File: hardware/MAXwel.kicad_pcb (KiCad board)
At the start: 2 copper layers, 85.9 x 94.6 mm, 155 parts, among them J1 Conn_02x05_Odd_Even, J2 Conn_02x12_Counter_Clockwise, J3 Barrel_Jack_Switch_Pin3Ring, SW1 SW_Push_Dual, SW10 SW_Wuerth_450301014042, SW11 SW_Wuerth_450301014042, SW12 SW_Wuerth_450301014042, SW13 SW_Wuerth_450301014042, SW2 SW_Push_Dual, SW3 SW_Push_Dual, SW4 SW_Push_Dual, SW5 SW_Wuerth_450301014042, SW6 SW_Wuerth_450301014042, SW7 SW_Wuerth_450301014042, SW8 SW_Wuerth_450301014042, SW9 SW_Push_DPDT, U1 D168K, U2 D168K, U3 D168K, U4 D168K, U5 EPM240T100, U6 AMS1117-3.3, X1 50.000, X2 14.756

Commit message: fill README with content + Rename project
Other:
- board text added: "MAXwel FPGA Board Michael Hohenstein"
- board text removed: "MAXwell FPGA Board Michael Hohenstein"

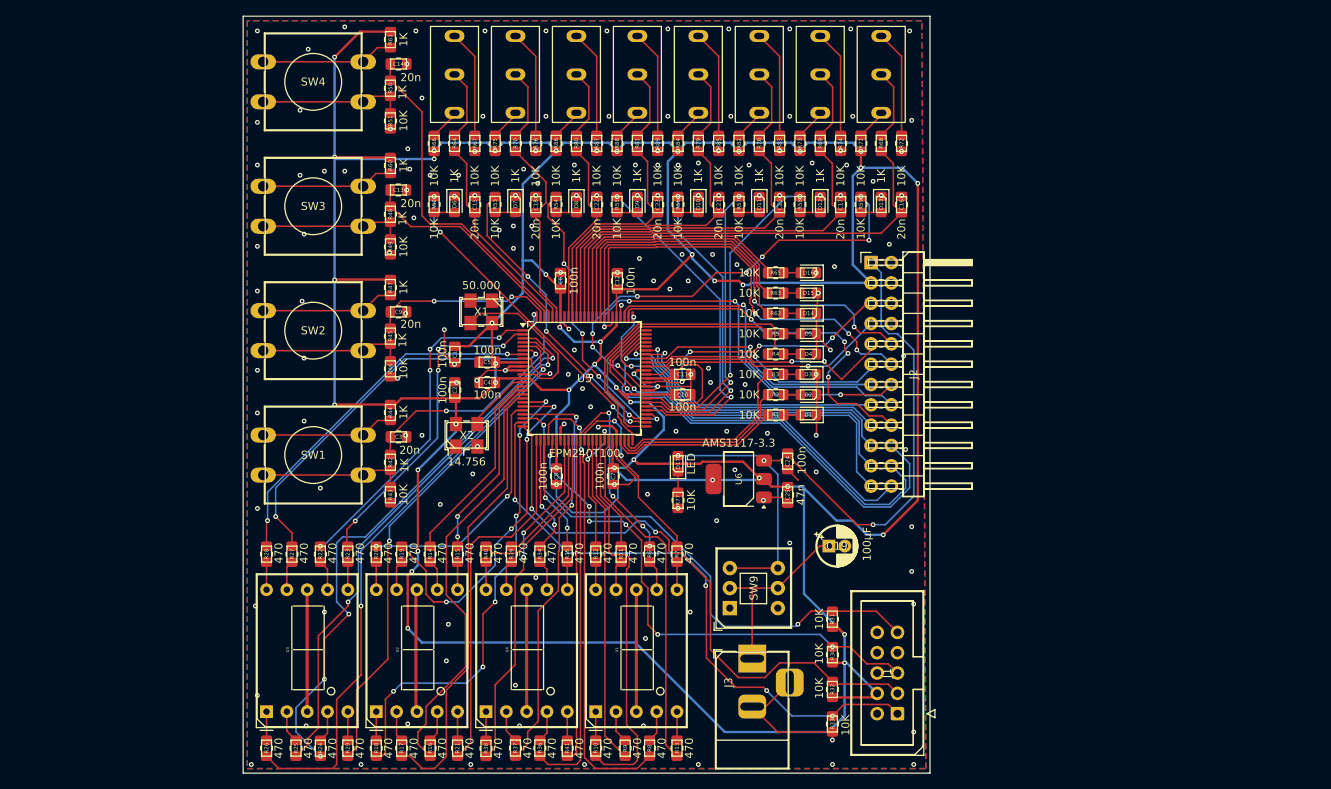
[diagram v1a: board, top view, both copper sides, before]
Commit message: fixed wrong footprint for slide switches
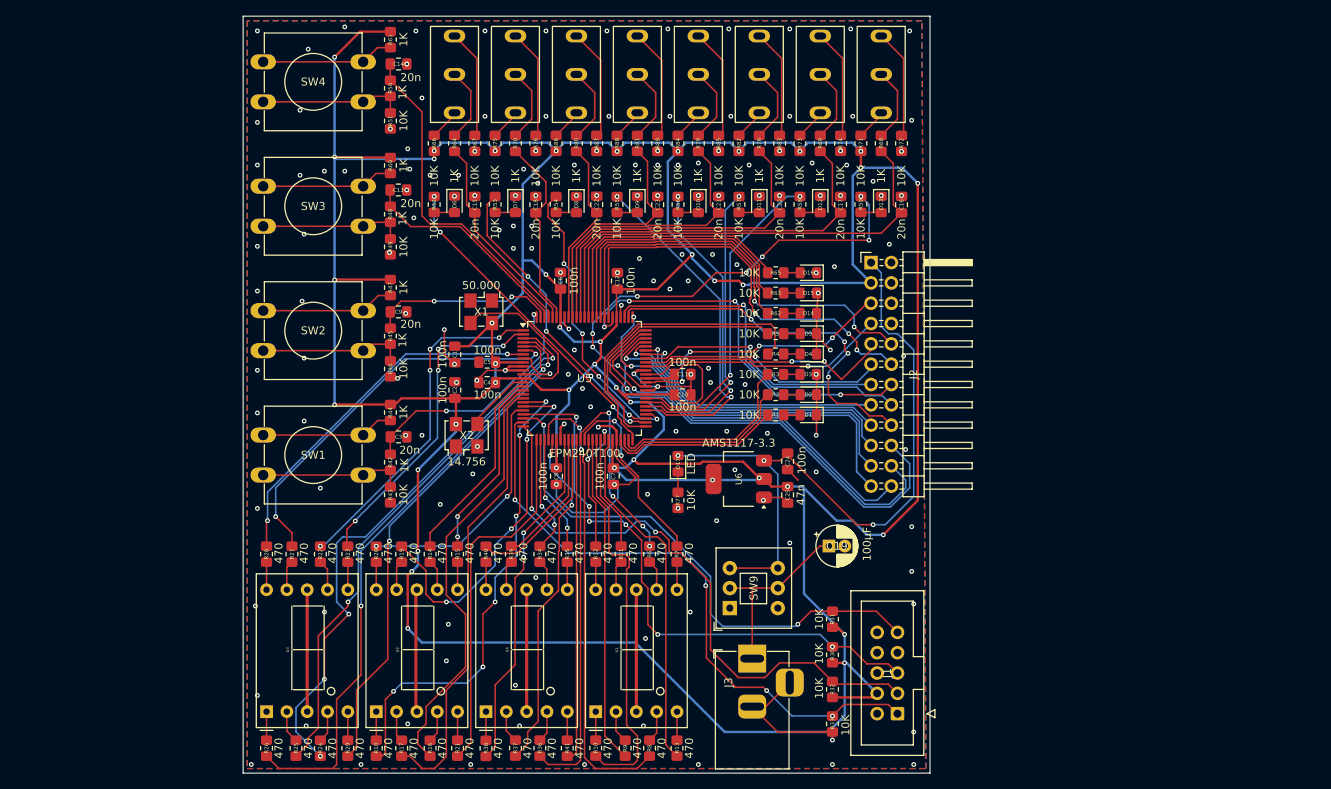
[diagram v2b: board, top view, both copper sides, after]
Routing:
- net Net-(SW12-B): track 8.90 -> 9.60 mm
- net Net-(SW10-B): track 8.90 -> 9.51 mm
- net Net-(SW13-B): track 8.90 -> 9.51 mm
- net Net-(SW11-B): track 8.90 -> 9.51 mm

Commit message: change resistor and capacitor size, rearrange pinheader and 7-seg connections
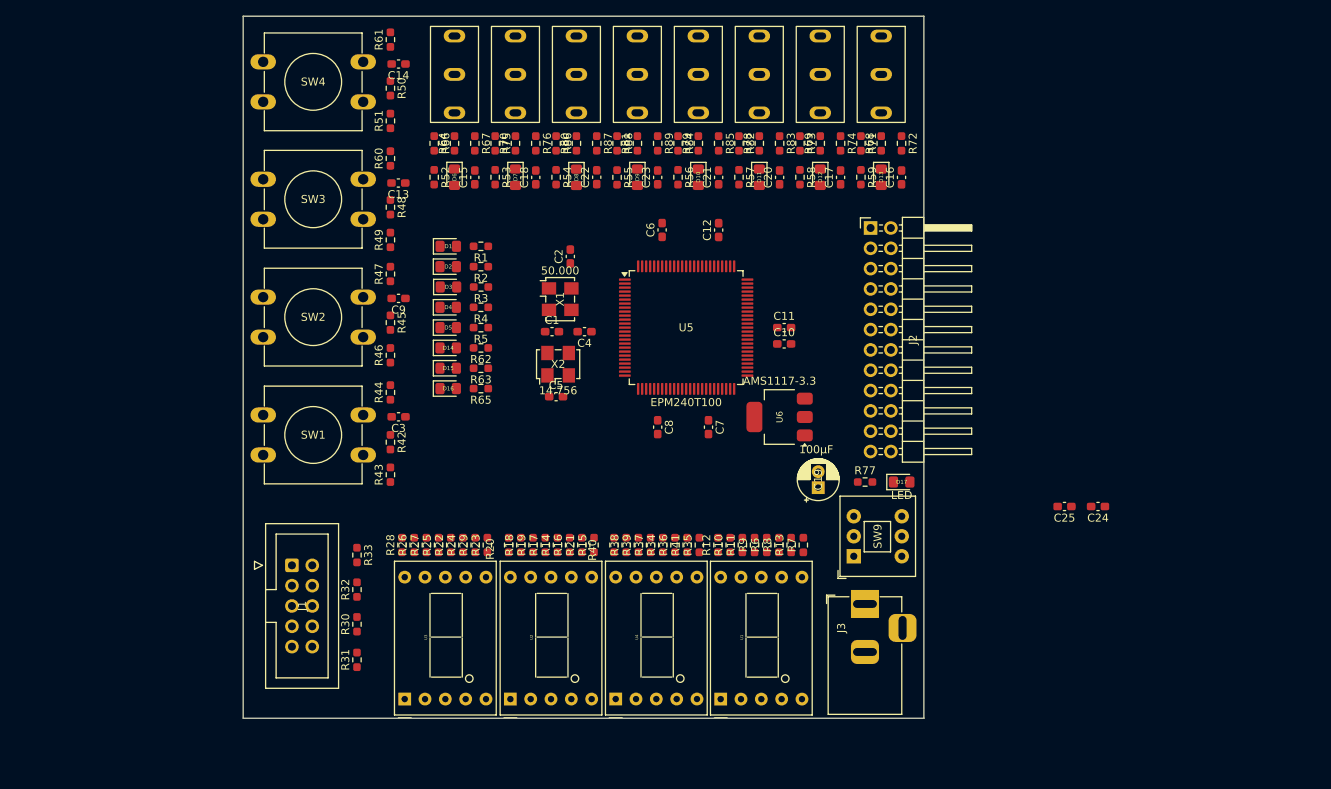
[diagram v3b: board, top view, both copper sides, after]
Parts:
- C1, C10, C11, C12, C13, C14, C15, C16, C17, C18, C2, C20, C21, C22, C23, C24, C25, C3, C4, C5, C6, C7, C8, C9: footprint Capacitor_SMD:C_0805_2012Metric_Pad1.18x1.45mm_HandSolder -> Capacitor_SMD:C_0603_1608Metric_Pad1.08x0.95mm_HandSolder
- R1, R10, R11, R12, R13, R14, R15, R16, R17, R18, R19, R2, R20, R21, R22, R23, R24, R25, R26, R27, R28, R29, R3, R30, R31, R32, R33, R34, R35, R36, R37, R38, R39, R4, R40, R41, R42, R43, R44, R45, R46, R47, R48, R49, R5, R50, R51, R52, R53, R54, R55, R56, R57, R58, R59, R6, R60, R61, R62, R63, R64, R65, R66, R67, R68, R69, R7, R70, R71, R72, R73, R74, R75, R76, R77, R78, R79, R8, R80, R81, R82, R83, R84, R85, R86, R87, R88, R89, R9: footprint Resistor_SMD:R_0805_2012Metric_Pad1.20x1.40mm_HandSolder -> Resistor_SMD:R_0603_1608Metric_Pad0.98x0.95mm_HandSolder
- moved J1 77.9 mm to (110.2, 88.9), turned to 0 degrees
- moved R33 63.1 mm to (118.4, 87.6), turned to -90 degrees
- moved R32 60.7 mm to (118.4, 91.9), turned to 90 degrees
- moved R31 59.7 mm to (118.4, 100.7), turned to 90 degrees
- moved R30 59.6 mm to (118.4, 96.3), turned to 90 degrees
- moved D1 49.7 mm to (129.8, 49.0), turned to 0 degrees
- moved D2 47.8 mm to (129.8, 51.6), turned to 0 degrees
- moved D16 47.3 mm to (129.8, 66.8), turned to 0 degrees
- moved D3 46.3 mm to (129.8, 54.1), turned to 0 degrees
- moved D15 46.0 mm to (129.8, 64.3), turned to 0 degrees
- moved D4 45.4 mm to (129.8, 56.6), turned to 0 degrees
- moved D14 45.2 mm to (129.8, 61.7), turned to 0 degrees
- moved D5 45.0 mm to (129.8, 59.2), turned to 0 degrees
- moved R1 42.5 mm to (133.9, 49.0), turned to 180 degrees
- moved R2 40.2 mm to (133.9, 51.6), turned to 180 degrees
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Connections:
- J2 pad 1: +5V -> Net-(J2-Pin_1)
- J2 pad 22: Net-(J2-Pin_22) -> +3V3
- J2 pad 24: Net-(J2-Pin_24) -> +5V
- J2 pad 3: +3V3 -> Net-(J2-Pin_3)
- R1 pad 1: Net-(U5-IO1_47) -> unconnected-(R1-Pad1)
- R10 pad 2: Net-(U5-IO1_41) -> Net-(U5-IO1_48)
- R11 pad 2: Net-(U5-IO1_42) -> Net-(U5-IO1_49)
- R12 pad 2: Net-(U5-IO1_43/DEV_OE) -> Net-(U5-IO1_50)
- R13 pad 2: Net-(U5-IO1_44/DEV_CLRn) -> Net-(U5-IO1_51)
- R14 pad 2: Net-(U5-IO1_15) -> Net-(U5-IO1_20)
- R15 pad 2: Net-(U5-IO1_16) -> Net-(U5-IO1_21)
- R16 pad 2: Net-(U5-IO1_17) -> Net-(U5-IO1_26)
- R17 pad 2: Net-(U5-IO1_18) -> Net-(U5-IO1_27)
- R18 pad 2: Net-(U5-IO1_19) -> Net-(U5-IO1_28)
- R19 pad 2: Net-(U5-IO1_20) -> Net-(U5-IO1_29)
- R2 pad 1: Net-(U5-IO1_48) -> unconnected-(R2-Pad1)
- R20 pad 2: Net-(U5-IO1_21) -> Net-(U5-IO1_30)
- R21 pad 2: Net-(U5-IO1_26) -> Net-(U5-IO1_33)
- R3 pad 1: Net-(U5-IO1_49) -> unconnected-(R3-Pad1)
- R34 pad 2: Net-(U5-IO1_27) -> Net-(U5-IO1_34)
- R35 pad 2: Net-(U5-IO1_28) -> Net-(U5-IO1_35)
- R36 pad 2: Net-(U5-IO1_29) -> Net-(U5-IO1_36)
- R37 pad 2: Net-(U5-IO1_30) -> Net-(U5-IO1_37)
- R38 pad 2: Net-(U5-IO1_33) -> Net-(U5-IO1_38)
- R39 pad 2: Net-(U5-IO1_34) -> Net-(U5-IO1_39)
- R4 pad 1: Net-(U5-IO1_50) -> unconnected-(R4-Pad1)
- R40 pad 2: Net-(U5-IO1_35) -> Net-(U5-IO1_40)
- R41 pad 2: Net-(U5-IO1_36) -> Net-(U5-IO1_41)
- R5 pad 1: Net-(U5-IO1_51) -> unconnected-(R5-Pad1)
- R52 pad 1: Net-(U5-IO2_52) -> unconnected-(R52-Pad1)
- R53 pad 1: Net-(U5-IO2_53) -> unconnected-(R53-Pad1)
- R54 pad 1: Net-(U5-IO2_54) -> unconnected-(R54-Pad1)
- R55 pad 1: Net-(U5-IO2_55) -> unconnected-(R55-Pad1)
- R56 pad 1: Net-(U5-IO2_56) -> unconnected-(R56-Pad1)
- R57 pad 1: Net-(U5-IO2_57) -> unconnected-(R57-Pad1)
- R58 pad 1: Net-(U5-IO2_58) -> unconnected-(R58-Pad1)
- R59 pad 1: Net-(U5-IO2_61) -> unconnected-(R59-Pad1)
- R6 pad 2: Net-(U5-IO1_37) -> Net-(U5-IO1_42)
- R7 pad 2: Net-(U5-IO1_38) -> Net-(U5-IO1_43/DEV_OE)
- R8 pad 2: Net-(U5-IO1_39) -> Net-(U5-IO1_44/DEV_CLRn)
- R9 pad 2: Net-(U5-IO1_40) -> Net-(U5-IO1_47)
- U5 pad 15: Net-(U5-IO1_15) -> unconnected-(U5-IO1_15-Pad15)
- U5 pad 16: Net-(U5-IO1_16) -> unconnected-(U5-IO1_16-Pad16)
- U5 pad 17: Net-(U5-IO1_17) -> unconnected-(U5-IO1_17-Pad17)
- U5 pad 18: Net-(U5-IO1_18) -> unconnected-(U5-IO1_18-Pad18)
- U5 pad 19: Net-(U5-IO1_19) -> unconnected-(U5-IO1_19-Pad19)
- U5 pad 52: Net-(U5-IO2_52) -> Net-(J2-Pin_23)
- U5 pad 53: Net-(U5-IO2_53) -> Net-(J2-Pin_21)
- U5 pad 54: Net-(U5-IO2_54) -> Net-(J2-Pin_20)
- U5 pad 55: Net-(U5-IO2_55) -> Net-(J2-Pin_19)
- U5 pad 56: Net-(U5-IO2_56) -> Net-(J2-Pin_18)
- U5 pad 57: Net-(U5-IO2_57) -> Net-(J2-Pin_17)
- U5 pad 58: Net-(U5-IO2_58) -> Net-(J2-Pin_16)
- U5 pad 61: Net-(U5-IO2_61) -> Net-(J2-Pin_15)
- U5 pad 62: Net-(J2-Pin_5) -> Net-(J2-Pin_14)
- U5 pad 64: Net-(J2-Pin_7) -> Net-(J2-Pin_13)
- U5 pad 66: Net-(J2-Pin_9) -> Net-(J2-Pin_12)
- U5 pad 68: Net-(J2-Pin_13) -> Net-(J2-Pin_10)
- U5 pad 69: Net-(J2-Pin_15) -> Net-(J2-Pin_9)
- U5 pad 70: Net-(J2-Pin_17) -> Net-(J2-Pin_7)
- U5 pad 71: Net-(J2-Pin_19) -> Net-(J2-Pin_5)
- U5 pad 72: Net-(J2-Pin_21) -> Net-(J2-Pin_3)
- U5 pad 73: Net-(J2-Pin_23) -> Net-(J2-Pin_1)
- U5 pad 74: Net-(J2-Pin_24) -> unconnected-(U5-IO2_74-Pad74)
- U5 pad 75: Net-(J2-Pin_22) -> unconnected-(U5-IO2_75-Pad75)
- U5 pad 76: Net-(J2-Pin_20) -> unconnected-(U5-IO2_76-Pad76)
- U5 pad 77: Net-(J2-Pin_18) -> unconnected-(U5-IO2_77-Pad77)
- U5 pad 78: Net-(J2-Pin_16) -> unconnected-(U5-IO2_78-Pad78)
- U5 pad 81: Net-(J2-Pin_14) -> unconnected-(U5-IO2_81-Pad81)
- U5 pad 82: Net-(J2-Pin_12) -> unconnected-(U5-IO2_82-Pad82)
- U5 pad 83: Net-(J2-Pin_10) -> unconnected-(U5-IO2_83-Pad83)
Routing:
- net +3V3: track 616.3 -> 0.00 mm, vias 42 -> 0
- net GND: track 168.8 -> 0.00 mm, vias 167 -> 0
- net +5V: track 87.4 -> 0.00 mm, vias 3 -> 0
- net Net-(J1-Pin_1): track 76.5 -> 0.00 mm, vias 4 -> 0
- net Net-(U5-IO1_5): track 74.6 -> 0.00 mm, vias 2 -> 0
- net Net-(J1-Pin_3): track 73.9 -> 0.00 mm, vias 2 -> 0
- net Net-(U5-IO1_3): track 72.8 -> 0.00 mm, vias 4 -> 0
- net Net-(J1-Pin_5): track 72.8 -> 0.00 mm, vias 6 -> 0
- net Net-(U5-IO1_4): track 67.5 -> 0.00 mm, vias 2 -> 0
- net Net-(J1-Pin_9): track 66.9 -> 0.00 mm, vias 2 -> 0
- net Net-(U5-IO1_8): track 63.5 -> 0.00 mm, vias 2 -> 0
- net Net-(U5-IO1_19): track 61.1 -> 0.00 mm, vias 6 -> 0
- net Net-(J2-Pin_20): track 59.5 -> 0.00 mm, vias 1 -> 0
- net Net-(U5-IO2_87): track 58.3 -> 0.00 mm
- net Net-(U5-IO2_61): track 56.4 -> 0.00 mm, vias 8 -> 0
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- removed copper zone on B.Cu, net GND
- removed copper zone on F.Cu, net GND
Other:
- board size 85.9 x 94.6 mm -> 85.1 x 87.8 mm

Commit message: rotation of FPGA
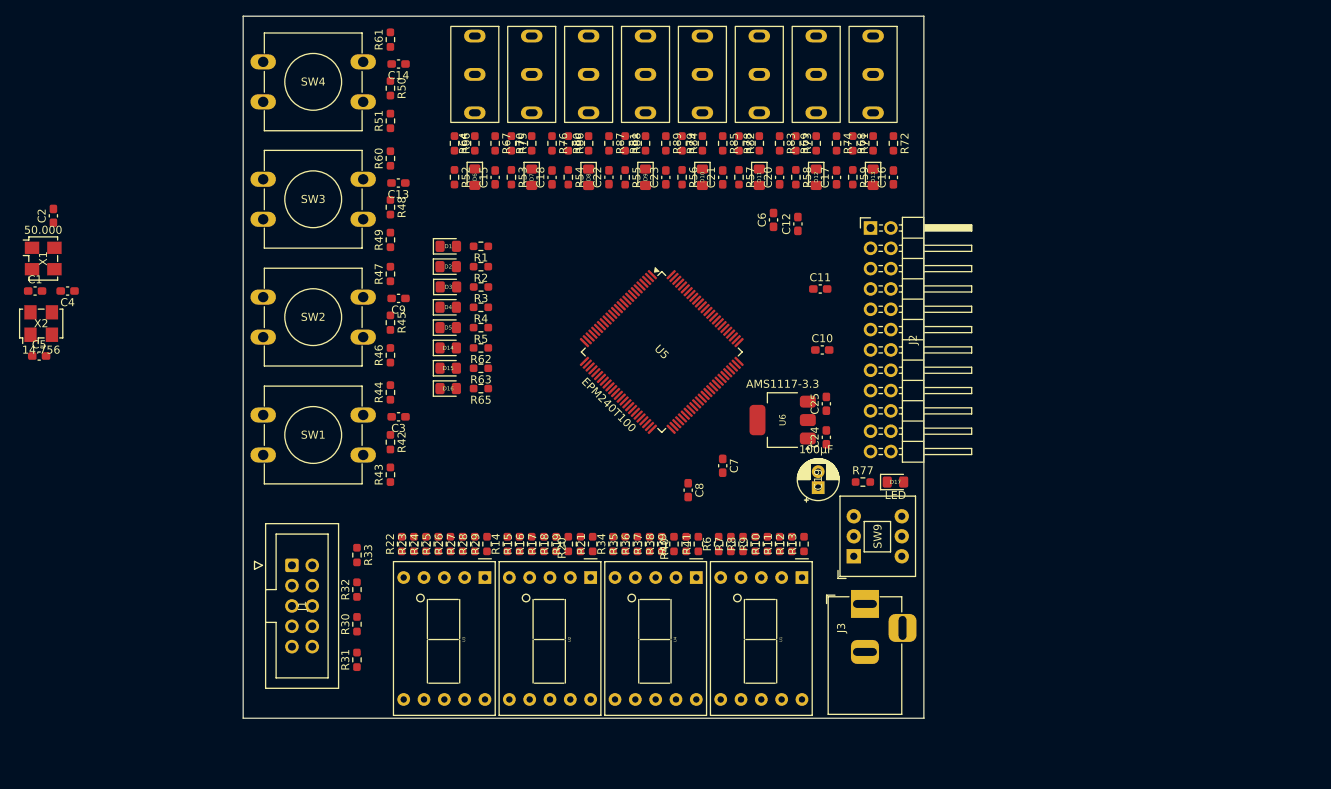
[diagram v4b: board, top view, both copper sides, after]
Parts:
- moved C4 64.8 mm to (82.2, 54.6)
- moved X1 64.8 mm to (79.1, 50.5)
- moved C5 64.8 mm to (78.6, 62.7)
- moved C1 64.8 mm to (78.1, 54.6)
- moved C2 64.8 mm to (80.4, 45.2)
- moved X2 64.8 mm to (78.9, 58.7)
- moved C24 35.0 mm to (177.0, 72.9), turned to 90 degrees
- moved C25 32.4 mm to (177.0, 68.7), turned to 90 degrees
- moved U1 18.3 mm to (174.0, 90.4), turned to -90 degrees
- moved U4 18.2 mm to (160.8, 90.4), turned to -90 degrees
- moved U2 18.2 mm to (147.6, 90.4), turned to -90 degrees
- moved U3 18.2 mm to (134.4, 90.4), turned to -90 degrees
- moved C6 14.0 mm to (170.4, 45.7)
- moved C12 9.94 mm to (173.5, 46.2)
- moved R15 9.31 mm to (138.7, 86.2)
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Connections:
- C13 pad 1: Net-(U5-IO2_98) -> Net-(C13-Pad1)
- C14 pad 1: Net-(U5-IO2_97) -> Net-(C14-Pad1)
- C15 pad 1: Net-(U5-IO2_96) -> Net-(C15-Pad1)
- C16 pad 1: Net-(U5-IO2_87) -> Net-(C16-Pad1)
- C17 pad 1: Net-(U5-IO2_88) -> Net-(C17-Pad1)
- C18 pad 1: Net-(U5-IO2_95) -> Net-(C18-Pad1)
- C20 pad 1: Net-(U5-IO2_89) -> Net-(C20-Pad1)
- C21 pad 1: Net-(U5-IO2_90) -> Net-(C21-Pad1)
- C22 pad 1: Net-(U5-IO2_92) -> Net-(C22-Pad1)
- C23 pad 1: Net-(U5-IO2_91) -> Net-(C23-Pad1)
- C3 pad 1: Net-(U5-IO2_100) -> Net-(C3-Pad1)
- C9 pad 1: Net-(U5-IO2_99) -> Net-(C9-Pad1)
- R10 pad 1: Net-(U1-E) -> Net-(U1-F)
- R10 pad 2: Net-(U5-IO1_48) -> Net-(U5-IO2_58)
- R11 pad 1: Net-(U1-F) -> Net-(U1-D)
- R11 pad 2: Net-(U5-IO1_49) -> Net-(U5-IO2_61)
- R12 pad 2: Net-(U5-IO1_50) -> Net-(U5-IO2_62/GCLK2)
- R13 pad 1: Net-(U1-DP) -> Net-(U1-E)
- R13 pad 2: Net-(U5-IO1_51) -> Net-(U5-IO2_64/GCLK3)
- R14 pad 1: Net-(U2-A) -> Net-(U2-DP)
- R14 pad 2: Net-(U5-IO1_20) -> Net-(U5-IO1_36)
- R15 pad 2: Net-(U5-IO1_21) -> Net-(U5-IO1_37)
- R16 pad 2: Net-(U5-IO1_26) -> Net-(U5-IO1_38)
- R17 pad 1: Net-(U2-D) -> Net-(U2-A)
- R17 pad 2: Net-(U5-IO1_27) -> Net-(U5-IO1_39)
- R18 pad 1: Net-(U2-E) -> Net-(U2-F)
- R18 pad 2: Net-(U5-IO1_28) -> Net-(U5-IO1_40)
- R19 pad 1: Net-(U2-F) -> Net-(U2-D)
- R19 pad 2: Net-(U5-IO1_29) -> Net-(U5-IO1_41)
- R20 pad 2: Net-(U5-IO1_30) -> Net-(U5-IO1_42)
- R21 pad 1: Net-(U2-DP) -> Net-(U2-E)
- R21 pad 2: Net-(U5-IO1_33) -> Net-(U5-IO1_43/DEV_OE)
- R22 pad 1: Net-(U3-A) -> Net-(U3-DP)
- R22 pad 2: Net-(U5-IO2_1) -> Net-(U5-IO1_26)
- R23 pad 2: Net-(U5-IO1_2) -> Net-(U5-IO1_27)
- R24 pad 2: Net-(U5-IO1_3) -> Net-(U5-IO1_28)
- R25 pad 1: Net-(U3-D) -> Net-(U3-A)
- R25 pad 2: Net-(U5-IO1_4) -> Net-(U5-IO1_29)
- R26 pad 1: Net-(U3-E) -> Net-(U3-F)
- R26 pad 2: Net-(U5-IO1_5) -> Net-(U5-IO1_30)
- R27 pad 1: Net-(U3-F) -> Net-(U3-D)
- R27 pad 2: Net-(U5-IO1_6) -> Net-(U5-IO1_33)
- R28 pad 2: Net-(U5-IO1_7) -> Net-(U5-IO1_34)
- R29 pad 1: Net-(U3-DP) -> Net-(U3-E)
- R29 pad 2: Net-(U5-IO1_8) -> Net-(U5-IO1_35)
- R34 pad 1: Net-(U4-A) -> Net-(U4-DP)
- R34 pad 2: Net-(U5-IO1_34) -> Net-(U5-IO1_44/DEV_CLRn)
- R35 pad 2: Net-(U5-IO1_35) -> Net-(U5-IO1_47)
- R36 pad 2: Net-(U5-IO1_36) -> Net-(U5-IO1_48)
- R37 pad 1: Net-(U4-D) -> Net-(U4-A)
- R37 pad 2: Net-(U5-IO1_37) -> Net-(U5-IO1_49)
- R38 pad 1: Net-(U4-E) -> Net-(U4-F)
- R38 pad 2: Net-(U5-IO1_38) -> Net-(U5-IO1_50)
- R39 pad 1: Net-(U4-F) -> Net-(U4-D)
- R39 pad 2: Net-(U5-IO1_39) -> Net-(U5-IO1_51)
- R40 pad 2: Net-(U5-IO1_40) -> Bridge_2
- R41 pad 1: Net-(U4-DP) -> Net-(U4-E)
- R41 pad 2: Net-(U5-IO1_41) -> Bridge_1
- R42 pad 1: Net-(U5-IO2_100) -> Net-(C3-Pad1)
- R45 pad 1: Net-(U5-IO2_99) -> Net-(C9-Pad1)
- R48 pad 1: Net-(U5-IO2_98) -> Net-(C13-Pad1)
- R50 pad 1: Net-(U5-IO2_97) -> Net-(C14-Pad1)
- R6 pad 1: Net-(U1-A) -> Net-(U1-DP)
- R6 pad 2: Net-(U5-IO1_42) -> Net-(U5-IO2_54)
- R62 pad 1: Net-(U5-IO2_84) -> unconnected-(R62-Pad1)
- R63 pad 1: Net-(U5-IO2_85) -> unconnected-(R63-Pad1)
- R64 pad 1: Net-(U5-IO2_96) -> Net-(C15-Pad1)
- R65 pad 1: Net-(U5-IO2_86) -> unconnected-(R65-Pad1)
- R68 pad 1: Net-(U5-IO2_87) -> Net-(C16-Pad1)
- R69 pad 1: Net-(U5-IO2_88) -> Net-(C17-Pad1)
- R7 pad 2: Net-(U5-IO1_43/DEV_OE) -> Net-(U5-IO2_55)
- R70 pad 1: Net-(U5-IO2_95) -> Net-(C18-Pad1)
- R78 pad 1: Net-(U5-IO2_89) -> Net-(C20-Pad1)
- R79 pad 1: Net-(U5-IO2_90) -> Net-(C21-Pad1)
- R8 pad 2: Net-(U5-IO1_44/DEV_CLRn) -> Net-(U5-IO2_56)
- R80 pad 1: Net-(U5-IO2_92) -> Net-(C22-Pad1)
- R81 pad 1: Net-(U5-IO2_91) -> Net-(C23-Pad1)
- R9 pad 1: Net-(U1-D) -> Net-(U1-A)
- R9 pad 2: Net-(U5-IO1_47) -> Net-(U5-IO2_57)
- U5 pad 1: Net-(U5-IO2_1) -> unconnected-(U5-IO2_1-Pad1)
- U5 pad 100: Net-(U5-IO2_100) -> unconnected-(U5-IO2_100-Pad100)
- U5 pad 2: Net-(U5-IO1_2) -> unconnected-(U5-IO1_2-Pad2)
- U5 pad 20: Net-(U5-IO1_20) -> unconnected-(U5-IO1_20-Pad20)
- U5 pad 21: Net-(U5-IO1_21) -> unconnected-(U5-IO1_21-Pad21)
- U5 pad 3: Net-(U5-IO1_3) -> unconnected-(U5-IO1_3-Pad3)
- U5 pad 4: Net-(U5-IO1_4) -> unconnected-(U5-IO1_4-Pad4)
- U5 pad 5: Net-(U5-IO1_5) -> unconnected-(U5-IO1_5-Pad5)
- U5 pad 52: Net-(J2-Pin_23) -> Bridge_1
- U5 pad 53: Net-(J2-Pin_21) -> Bridge_2
- U5 pad 54: Net-(J2-Pin_20) -> Net-(U5-IO2_54)
- U5 pad 55: Net-(J2-Pin_19) -> Net-(U5-IO2_55)
- U5 pad 56: Net-(J2-Pin_18) -> Net-(U5-IO2_56)
- U5 pad 57: Net-(J2-Pin_17) -> Net-(U5-IO2_57)
- U5 pad 58: Net-(J2-Pin_16) -> Net-(U5-IO2_58)
- U5 pad 6: Net-(U5-IO1_6) -> unconnected-(U5-IO1_6-Pad6)
- U5 pad 61: Net-(J2-Pin_15) -> Net-(U5-IO2_61)
- U5 pad 62: Net-(J2-Pin_14) -> Net-(U5-IO2_62/GCLK2)
- U5 pad 64: Net-(J2-Pin_13) -> Net-(U5-IO2_64/GCLK3)
- U5 pad 66: Net-(J2-Pin_12) -> Net-(J2-Pin_23)
- U5 pad 67: Net-(J2-Pin_11) -> Net-(J2-Pin_21)
- U5 pad 68: Net-(J2-Pin_10) -> Net-(J2-Pin_20)
- U5 pad 69: Net-(J2-Pin_9) -> Net-(J2-Pin_19)
- U5 pad 7: Net-(U5-IO1_7) -> unconnected-(U5-IO1_7-Pad7)
- U5 pad 70: Net-(J2-Pin_7) -> Net-(J2-Pin_18)
- U5 pad 71: Net-(J2-Pin_5) -> Net-(J2-Pin_17)
- U5 pad 72: Net-(J2-Pin_3) -> Net-(J2-Pin_16)
- U5 pad 73: Net-(J2-Pin_1) -> Net-(J2-Pin_15)
- U5 pad 74: unconnected-(U5-IO2_74-Pad74) -> Net-(J2-Pin_14)
- U5 pad 75: unconnected-(U5-IO2_75-Pad75) -> Net-(J2-Pin_13)
- U5 pad 76: unconnected-(U5-IO2_76-Pad76) -> Net-(J2-Pin_12)
- U5 pad 77: unconnected-(U5-IO2_77-Pad77) -> Net-(J2-Pin_11)
- U5 pad 78: unconnected-(U5-IO2_78-Pad78) -> Net-(J2-Pin_10)
- U5 pad 8: Net-(U5-IO1_8) -> unconnected-(U5-IO1_8-Pad8)
- U5 pad 81: unconnected-(U5-IO2_81-Pad81) -> Net-(J2-Pin_9)
- U5 pad 82: unconnected-(U5-IO2_82-Pad82) -> Net-(J2-Pin_7)
- U5 pad 83: unconnected-(U5-IO2_83-Pad83) -> Net-(J2-Pin_5)
- U5 pad 84: Net-(U5-IO2_84) -> Net-(J2-Pin_3)
- U5 pad 85: Net-(U5-IO2_85) -> Net-(J2-Pin_1)
- U5 pad 86: Net-(U5-IO2_86) -> unconnected-(U5-IO2_86-Pad86)
- U5 pad 87: Net-(U5-IO2_87) -> unconnected-(U5-IO2_87-Pad87)
- U5 pad 88: Net-(U5-IO2_88) -> unconnected-(U5-IO2_88-Pad88)
- U5 pad 89: Net-(U5-IO2_89) -> unconnected-(U5-IO2_89-Pad89)
- U5 pad 90: Net-(U5-IO2_90) -> unconnected-(U5-IO2_90-Pad90)
- U5 pad 91: Net-(U5-IO2_91) -> unconnected-(U5-IO2_91-Pad91)
- U5 pad 92: Net-(U5-IO2_92) -> unconnected-(U5-IO2_92-Pad92)
- U5 pad 95: Net-(U5-IO2_95) -> unconnected-(U5-IO2_95-Pad95)
- U5 pad 96: Net-(U5-IO2_96) -> unconnected-(U5-IO2_96-Pad96)
- U5 pad 97: Net-(U5-IO2_97) -> unconnected-(U5-IO2_97-Pad97)
- U5 pad 98: Net-(U5-IO2_98) -> unconnected-(U5-IO2_98-Pad98)
- U5 pad 99: Net-(U5-IO2_99) -> unconnected-(U5-IO2_99-Pad99)
